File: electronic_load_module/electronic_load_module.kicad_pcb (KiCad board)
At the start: 2 copper layers, 86.9 x 35.3 mm, 66 parts, among them J1 Conn_01x03_Pin, J10 Conn_01x02_Pin, J2 Conn_01x03_Pin, J3 Conn_01x04_Pin, J4 Screw_Terminal_01x02, J5 Screw_Terminal_01x02, J6 Conn_01x05_Pin, J7 Conn_01x04_Pin, J8 Conn_01x04_Pin, J9 Conn_01x04_Pin, Q1 TIP142, Q2 TIP142, Q3 BC549, Q4 BC549, U1 NCS21804, U2 MCP9700Ax-ETT, U3 SN74LV4052, U4 INA180A1, U5 SN74LV4052, U6 NCS21804, U7 INA180A1

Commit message: IDeo ok
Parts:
- removed J1: Conn_01x03_Pin, Connector_PinHeader_2.54mm:PinHeader_1x03_P2.54mm_Vertical
- removed J3: Conn_01x04_Pin, Connector_PinHeader_2.54mm:PinHeader_1x04_P2.54mm_Vertical
- removed J4: Screw_Terminal_01x02, TerminalBlock:TerminalBlock_Altech_AK300-2_P5.00mm
- removed Q1, Q2: TIP142, Package_TO_SOT_THT:TO-247-3_Vertical
- removed Q3: BC549, Package_TO_SOT_THT:TO-92_Inline
- removed R10, R17, R20, R23, R24, R25, R28, R29, R34, R35, R36: 0, Resistor_SMD:R_0603_1608Metric_Pad0.98x0.95mm_HandSolder
- removed R13, R14, R18, R19: 10k, Resistor_SMD:R_0603_1608Metric_Pad0.98x0.95mm_HandSolder
- removed R15, R6: 0.05, Resistor_SMD:R_2512_6332Metric_Pad1.40x3.35mm_HandSolder
- removed R16: 220, Resistor_SMD:R_0603_1608Metric_Pad0.98x0.95mm_HandSolder
- removed R21, R22: 1k, Resistor_SMD:R_0603_1608Metric_Pad0.98x0.95mm_HandSolder
- removed U3: SN74LV4052, Package_SO:SOIC-16_3.9x9.9mm_P1.27mm
- removed U4: INA180A1, Package_TO_SOT_SMD:SOT-23-5
- added C10: 100n, Capacitor_SMD:C_0603_1608Metric_Pad1.08x0.95mm_HandSolder, F.Cu at (58.7, 67.5)
- added J11: Conn_01x03_Pin, Connector_PinHeader_2.54mm:PinHeader_1x03_P2.54mm_Vertical, F.Cu at (50.8, 51.3)
- added Q5: TIP142, Package_TO_SOT_THT:TO-247-3_Vertical, F.Cu at (65.2, 34.8)
- added R43: 1k, Resistor_SMD:R_0603_1608Metric_Pad0.98x0.95mm_HandSolder, F.Cu at (79.0, 46.0)
- added U8: INA180A1, Package_TO_SOT_SMD:SOT-23-5, F.Cu at (60.0, 39.2)
- C1: value 220p -> 100p; moved to F.Cu
- C2, C7: value 10n -> 100n; moved to F.Cu
- C3, C6, J2, R30, R31, R9, U1, U5, U7: moved to F.Cu
- C4: value 100n -> 100p; moved to F.Cu
- C5: value 220p -> 100n; moved to F.Cu
- C8, C9: value 100n -> 220p; moved to F.Cu
- J10: value Conn_01x02_Pin -> Conn_01x05_Pin; footprint Connector_PinHeader_2.54mm:PinHeader_1x02_P2.54mm_Vertical -> Connector_JST:JST_EH_B5B-EH-A_1x05_P2.50mm_Vertical; moved to F.Cu
- J5: value Screw_Terminal_01x02 -> Conn_01x03_Pin; footprint TerminalBlock:TerminalBlock_Altech_AK300-2_P5.00mm -> Connector_JST:JST_EH_B3B-EH-A_1x03_P2.50mm_Vertical; moved to F.Cu
- J6: footprint Connector_PinHeader_2.54mm:PinHeader_1x05_P2.54mm_Vertical -> Connector_JST:JST_EH_B5B-EH-A_1x05_P2.50mm_Vertical; moved to F.Cu
- J7: value Conn_01x04_Pin -> Conn_01x03_Pin; footprint Connector_PinHeader_2.54mm:PinHeader_1x04_P2.54mm_Vertical -> Connector_JST:JST_EH_B3B-EH-A_1x03_P2.50mm_Vertical; moved to F.Cu
- J8, J9: value Conn_01x04_Pin -> Conn_01x02_Socket; footprint Connector_PinHeader_2.54mm:PinHeader_1x04_P2.54mm_Vertical -> Connector_JST:JST_EH_B2B-EH-A_1x02_P2.50mm_Vertical; moved to F.Cu
- Q4: value BC549 -> TIP142; footprint Package_TO_SOT_THT:TO-92_Inline -> Package_TO_SOT_THT:TO-247-3_Vertical; moved to F.Cu
- R1, R26, R27: value 0 -> 10k; moved to F.Cu
- R11: value 0 -> 220; moved to F.Cu
- R12: value 1k -> 0; moved to F.Cu
- R2: value 10k -> 90k; moved to F.Cu
- R3: value 220 -> 3.3k; moved to F.Cu
- R32, R33: value 0 -> 0.05; footprint Resistor_SMD:R_0603_1608Metric_Pad0.98x0.95mm_HandSolder -> Resistor_SMD:R_2512_6332Metric_Pad1.40x3.35mm_HandSolder; moved to F.Cu
- R4: value 280k -> 6.6k; moved to F.Cu
- R5: value 0 -> 100; moved to F.Cu
- R7: value 20k -> 10k; moved to F.Cu
- R8: value 10k -> 220; moved to F.Cu
- U2: value MCP9700Ax-ETT -> TLV07; footprint Package_TO_SOT_THT:TO-92_Inline -> Package_SO:SOIC-8_3.9x4.9mm_P1.27mm
- U6: value NCS21804 -> SN74LV4052; footprint Package_SO:TSSOP-14_4.4x5mm_P0.65mm -> Package_SO:SOIC-16_3.9x9.9mm_P1.27mm; moved to F.Cu
- moved U6 142.1 mm to (50.6, 45.6), turned to -90 degrees
- moved J6 136.9 mm to (35.5, 51.9), turned to 90 degrees
- moved C5 136.2 mm to (54.4, 50.2), turned to 180 degrees
- moved R27 135.0 mm to (52.4, 39.2)
- moved R30 131.9 mm to (45.1, 39.2), turned to 180 degrees
- moved C8 131.3 mm to (65.8, 45.5), turned to 0 degrees
- moved C7 130.3 mm to (60.0, 43.5), turned to 0 degrees
- moved C9 128.7 mm to (48.8, 39.2), turned to 180 degrees
- moved R8 126.1 mm to (65.8, 48.6)
- moved J5 124.4 mm to (45.2, 71.0), turned to 90 degrees
- moved U2 119.9 mm to (63.4, 64.8), turned to 0 degrees
- moved R26 109.9 mm to (72.2, 40.0), turned to 90 degrees
- moved U5 109.5 mm to (72.8, 45.9), turned to -90 degrees
- moved J7 106.2 mm to (67.0, 57.8)
- moved R11 106.2 mm to (41.4, 42.6), turned to 0 degrees
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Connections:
- C1 pad 1: Net-(U1C--) -> Net-(U1C-+)
- C1 pad 2: Net-(C1-Pad2) -> 0
- C2 pad 1: Net-(U1B-+) -> 5V
- C4 pad 1: 5V -> Net-(U1B-+)
- C5 pad 1: Net-(U5-Y) -> 5V
- C5 pad 2: Net-(C5-Pad2) -> 0
- C7 pad 1: Net-(U6B-+) -> 5V
- C8 pad 1: 5V -> Net-(U1D--)
- C8 pad 2: 0 -> Net-(C8-Pad2)
- C9 pad 1: 5V -> Net-(U1A--)
- C9 pad 2: 0 -> Net-(C9-Pad2)
- J10 pad 2: 0 -> COMMON_MUX_A
- J2 pad 1: DAC_from_board -> DAC_2
- J2 pad 2: ADC_SHUNT -> Net-(J2-Pin_2)
- J2 pad 3: ENABLE -> MIXER
- J5 pad 1: 0 -> input_10
- J5 pad 2: input -> input_1000
- J6 pad 1: COMMON_MUX_A -> 5V
- J6 pad 2: COMMON_MUX_B -> COMMON_MUX_A
- J6 pad 3: TEMP -> COMMON_MUX_B
- J6 pad 5: DIVIDER -> 0
- J7 pad 1: DAC_2 -> input_sense
- J7 pad 2: Net-(J7-Pin_2) -> unconnected-(J7-Pin_2-Pad2)
- J8 pad 1: SHUNT -> DAC_from_board
- J8 pad 2: Net-(J8-Pin_2) -> SHUNT
- J9 pad 1: DAC -> DAC_from_board_2
- J9 pad 2: Net-(J9-Pin_2) -> SHUNT_2
- Q4 pad 1: Net-(Q1-B) -> Net-(Q4-B)
- Q4 pad 2: Net-(Q4-B) -> input
- Q4 pad 3: 0 -> Net-(Q4-E)
- R1 pad 1: Net-(C1-Pad2) -> 0
- R1 pad 2: Net-(Q1-B) -> DAC
- R11 pad 1: Net-(U1B--) -> DAC_from_board
- R11 pad 2: DAC -> Net-(U1B-+)
- R12 pad 1: 0 -> Net-(U1B--)
- R12 pad 2: DIVIDER -> DAC
- R2 pad 1: 0 -> input_sense
- R2 pad 2: ADC_SHUNT -> input_10
- R26 pad 1: DAC_2 -> SHUNT_2
- R26 pad 2: Net-(J3-Pin_3) -> Net-(U1D--)
- R27 pad 1: SHUNT_2 -> SHUNT
- R27 pad 2: Net-(J3-Pin_4) -> Net-(U1A--)
- R3 pad 1: DAC_from_board -> input_10
- R3 pad 2: Net-(U1B-+) -> DIVIDER_R
- R30 pad 1: DAC_2 -> Net-(C9-Pad2)
- R30 pad 2: Net-(J7-Pin_4) -> Net-(Q4-B)
- R31 pad 1: DIVIDER -> Net-(C8-Pad2)
- R31 pad 2: Net-(J9-Pin_2) -> Net-(Q5-B)
- R32 pad 1: DIVIDER -> Net-(Q4-E)
- R32 pad 2: Net-(J9-Pin_3) -> 0
- R33 pad 1: DAC -> Net-(Q5-E)
- R33 pad 2: Net-(J9-Pin_4) -> 0
- R4 pad 1: input_sense -> DIVIDER_R
- R4 pad 2: input_divider -> input_1000
- R5 pad 1: ADC_SHUNT -> input_1000
- R5 pad 2: Net-(U1D--) -> Net-(J7-Pin_3)
- R7 pad 1: input_divider -> 0
- R7 pad 2: 0 -> DAC_2
- R8 pad 1: SHUNT_2 -> DAC_from_board_2
- R8 pad 2: Net-(U5-Y) -> Net-(U1C-+)
- R9 pad 1: Net-(U1A--) -> Net-(U1C--)
- R9 pad 2: DIVIDER -> DAC_2
- U1 pad 1: DIVIDER -> Net-(C9-Pad2)
- U1 pad 12: SHUNT -> Net-(U1D-+)
- U1 pad 14: ADC_SHUNT -> Net-(C8-Pad2)
- U1 pad 3: input_divider -> Net-(U1A-+)
- U1 pad 8: Net-(C1-Pad2) -> DAC_2
- U2 pad 1: 5V -> (no net)
- U2 pad 2: Net-(U2-V_{OUT}) -> DIVIDER
- U2 pad 3: 0 -> DIVIDER_R
- U5 pad 11: Net-(J7-Pin_4) -> Net-(J2-Pin_2)
- U5 pad 13: Net-(U5-X) -> Net-(U1D-+)
- U5 pad 14: Net-(J7-Pin_2) -> Net-(J2-Pin_2)
- U5 pad 15: Net-(J7-Pin_3) -> DIVIDER
- U5 pad 2: Net-(J3-Pin_3) -> DAC_2
- U5 pad 3: Net-(U5-Y) -> Net-(U1D--)
- U5 pad 4: Net-(J3-Pin_4) -> SHUNT_2
- U5 pad 5: Net-(J3-Pin_2) -> SHUNT_2
- U6 pad 1: TEMP -> SHUNT
- U6 pad 10: Net-(U5-X) -> COMMON_MUX_A
- U6 pad 11: 0 -> Net-(J11-Pin_2)
- U6 pad 12: SHUNT_2 -> DAC
- U6 pad 13: Net-(U6D--) -> Net-(U1A-+)
- U6 pad 14: ADC_SHUNT_2 -> Net-(J11-Pin_2)
- U6 pad 2: Net-(U6A--) -> DAC
- U6 pad 3: Net-(U6A-+) -> Net-(U1A--)
- U6 pad 4: 5V -> SHUNT
- U6 pad 5: Net-(U6B-+) -> SHUNT
- U6 pad 6: Net-(U6B--) -> 0
- U6 pad 7: DAC_2 -> 0
- U6 pad 8: Net-(C5-Pad2) -> 0
- U6 pad 9: Net-(U5-Y) -> COMMON_MUX_B
- U7 pad 1: SHUNT -> SHUNT_2
- U7 pad 3: Net-(Q1-E) -> Net-(Q5-E)
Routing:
- net 5V: track 148.7 -> 0.00 mm, vias 7 -> 0
- net DIVIDER: track 84.0 -> 0.00 mm, vias 4 -> 0
- net COMMON_MUX_A: track 65.8 -> 0.00 mm, vias 3 -> 0
- net Net-(Q2-E): track 57.6 -> 0.00 mm
- net COMMON_MUX_B: track 55.7 -> 0.00 mm, vias 1 -> 0
- net SHUNT: track 43.3 -> 0.00 mm, vias 3 -> 0
- net DAC: track 35.5 -> 0.00 mm, vias 3 -> 0
- net DAC_2: track 34.5 -> 0.00 mm
- net SHUNT_2: track 32.5 -> 0.00 mm, vias 4 -> 0
- net TEMP: track 28.3 -> 0.00 mm, vias 1 -> 0
- net Net-(U2-V_{OUT}): track 25.5 -> 0.00 mm
- net Net-(U1C-+): track 24.0 -> 0.00 mm, vias 2 -> 0
- net Net-(J9-Pin_4): track 21.9 -> 0.00 mm
- net Net-(Q1-E): track 21.1 -> 0.00 mm, vias 1 -> 0
- net Net-(U1C--): track 18.7 -> 0.00 mm, vias 2 -> 0
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- removed copper zone on B.Cu, net 0
- removed copper zone on F.Cu, net 0
- removed copper zone on B.Cu, net Net-(Q1-E)
- removed copper zone on F.Cu, net Net-(Q1-E)
- removed copper zone on B.Cu, net Net-(Q2-E)
- removed copper zone on F.Cu, net Net-(Q2-E)
- removed copper zone on B.Cu, net input
- removed copper zone on F.Cu, net input
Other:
- board outline removed

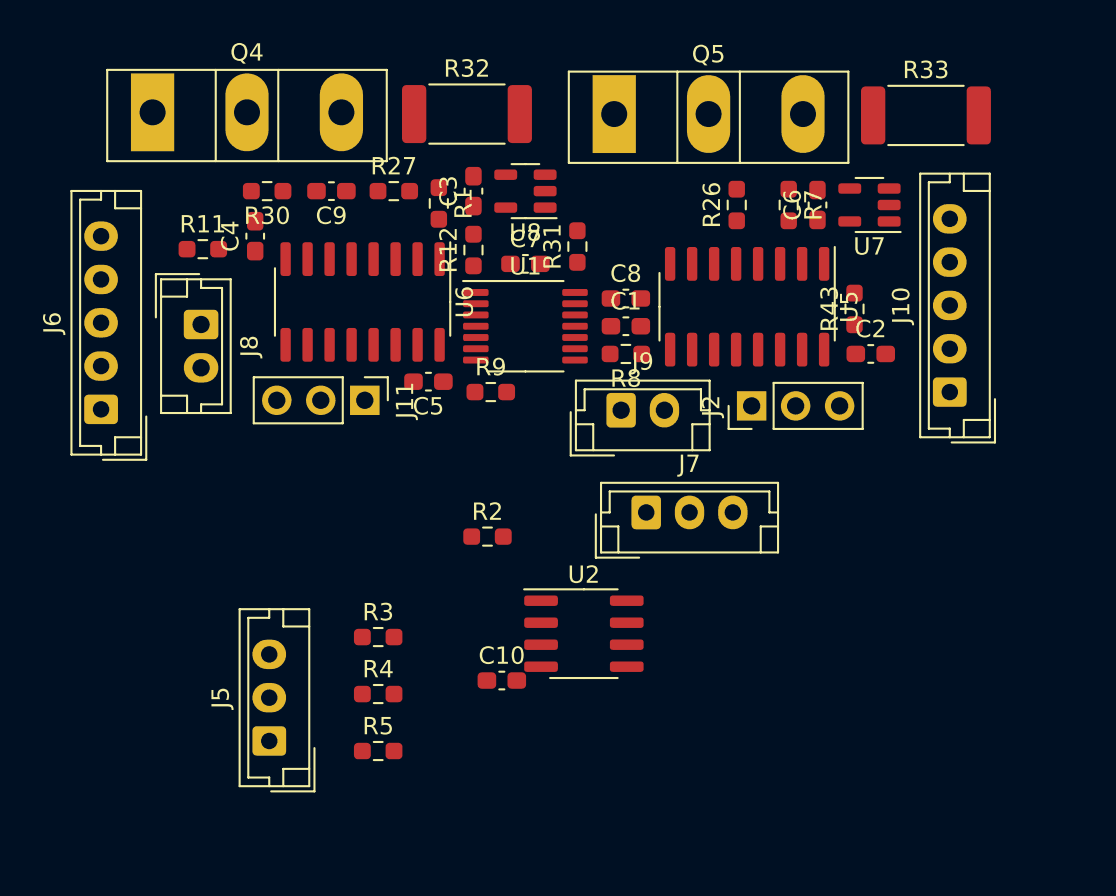
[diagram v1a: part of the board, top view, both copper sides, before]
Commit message: Konačno PCB za BJT modul je počeo.
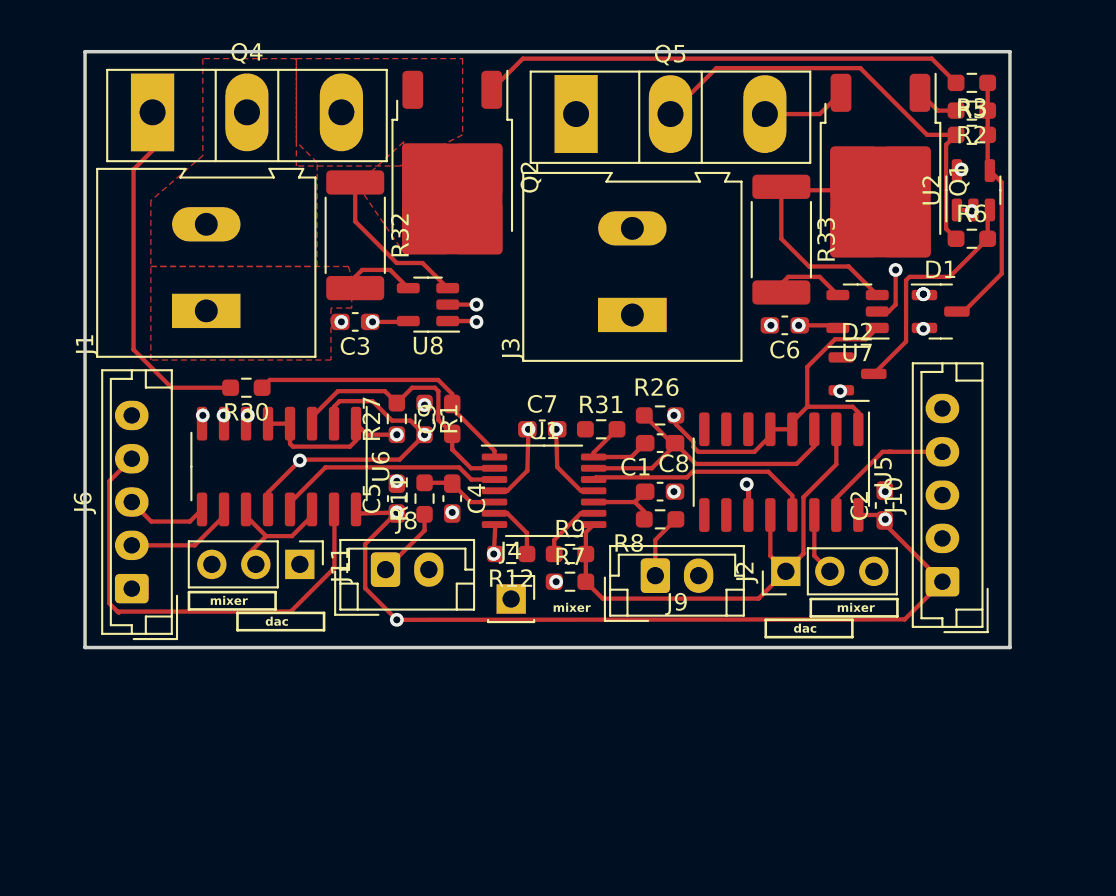
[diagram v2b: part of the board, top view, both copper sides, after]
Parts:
- removed C10: 100n, Capacitor_SMD:C_0603_1608Metric_Pad1.08x0.95mm_HandSolder
- removed J5, J7: Conn_01x03_Pin, Connector_JST:JST_EH_B3B-EH-A_1x03_P2.50mm_Vertical
- removed R4: 6.6k, Resistor_SMD:R_0603_1608Metric_Pad0.98x0.95mm_HandSolder
- removed R43: 1k, Resistor_SMD:R_0603_1608Metric_Pad0.98x0.95mm_HandSolder
- added D1: BAT54S, Package_TO_SOT_SMD:SOT-23, F.Cu at (84.0, 46.2)
- added D2: BAT54S, Package_TO_SOT_SMD:SOT-23, F.Cu at (79.2, 49.8)
- added J1: Screw_Terminal_01x02, TerminalBlock:TerminalBlock_Altech_AK300-2_P5.00mm, F.Cu at (41.6, 46.2)
- added J3: Screw_Terminal_01x02, TerminalBlock:TerminalBlock_Altech_AK300-2_P5.00mm, F.Cu at (66.2, 46.4)
- added J4: Conn_01x01_Socket, Connector_PinSocket_2.54mm:PinSocket_1x01_P2.54mm_Vertical, F.Cu at (59.2, 62.8)
- added Q1: DMT10H025SK3-13, Package_TO_SOT_SMD:TO-252-2, F.Cu at (80.5, 38.6)
- added Q2: DMT10H025SK3-13, Package_TO_SOT_SMD:TO-252-2, F.Cu at (55.8, 38.4)
- added R6: 10k, Resistor_SMD:R_0603_1608Metric_Pad0.98x0.95mm_HandSolder, F.Cu at (85.8, 42.0)
- C1, C4: value 100p -> 1n
- R2: value 90k -> 100
- R3: value 3.3k -> 100
- R30, R31: value 0 -> 3.3k
- R5: value 100 -> 10k
- U2: value TLV07 -> MCP6541; footprint Package_SO:SOIC-8_3.9x4.9mm_P1.27mm -> Package_TO_SOT_SMD:SOT-23-5
- moved R5 49.4 mm to (85.8, 36.0)
- moved R3 46.9 mm to (85.8, 33.0), turned to 180 degrees
- moved R2 37.2 mm to (85.8, 34.6), turned to 180 degrees
- moved U2 34.1 mm to (85.9, 39.2), turned to 90 degrees
- moved R7 25.1 mm to (62.6, 61.8), turned to 0 degrees
- moved R11 19.3 mm to (54.2, 57.0), turned to 90 degrees
- moved C4 18.9 mm to (55.8, 57.0), turned to -90 degrees
- moved J8 17.7 mm to (52.0, 61.1), turned to 0 degrees
- moved R12 17.7 mm to (59.2, 60.2), turned to 180 degrees
- moved C9 14.9 mm to (55.8, 52.4), turned to 90 degrees
- moved R27 13.2 mm to (52.6, 52.4), turned to 90 degrees
- moved R26 12.9 mm to (67.8, 52.2), turned to 180 degrees
- moved R1 12.5 mm to (54.2, 52.4)
- moved R30 11.4 mm to (43.9, 50.6)
- moved R33 11.0 mm to (74.8, 42.0), turned to -90 degrees
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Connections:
- Q4 pad 3: Net-(Q4-E) -> Net-(Q2-S)
- Q5 pad 3: Net-(Q5-E) -> Net-(Q1-S)
- R2 pad 1: input_sense -> P_GATE
- R2 pad 2: input_10 -> Net-(Q1-G)
- R3 pad 1: input_10 -> P_GATE
- R3 pad 2: DIVIDER_R -> Net-(Q2-G)
- R32 pad 1: Net-(Q4-E) -> Net-(Q2-D)
- R33 pad 1: Net-(Q5-E) -> Net-(Q1-D)
- R5 pad 1: input_1000 -> input
- R5 pad 2: Net-(J7-Pin_3) -> P_GATE
- U2 pad 1: (no net) -> 0
- U2 pad 2: DIVIDER -> 0
- U2 pad 3: DIVIDER_R -> Net-(D2-COM)
- U2 pad 4: 0 -> P_GATE
- U2 pad 5: (no net) -> 5V
- U7 pad 3: Net-(Q5-E) -> Net-(Q1-D)
- U8 pad 3: Net-(Q4-E) -> Net-(Q2-D)
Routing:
- net 5V: track 0.00 -> 167.1 mm, vias 0 -> 8
- net DIVIDER: track 0.00 -> 82.9 mm
- net COMMON_MUX_A: track 0.00 -> 53.9 mm
- net COMMON_MUX_B: track 0.00 -> 52.0 mm
- net MIXER: track 0.00 -> 39.7 mm
- net DAC: track 0.00 -> 36.1 mm, vias 0 -> 3
- net SHUNT_2: track 0.00 -> 31.8 mm, vias 0 -> 1
- net DAC_2: track 0.00 -> 29.4 mm
- net SHUNT: track 0.00 -> 28.9 mm, vias 0 -> 2
- net Net-(Q2-G): track 0.00 -> 28.1 mm
- net input: track 0.00 -> 25.4 mm
- net Net-(Q4-B): track 0.00 -> 20.7 mm
- net 0: track 0.00 -> 19.5 mm, vias 0 -> 18
- net Net-(U1D--): track 0.00 -> 17.7 mm
- net Net-(C9-Pad2): track 0.00 -> 16.1 mm
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- added copper zone on B.Cu, net 0
- added copper zone on F.Cu, net 0
- added copper zone on F.Cu, net Net-(Q2-D)
- added copper zone on F.Cu, net Net-(Q2-S)
- added copper zone on F.Cu, net input
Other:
- board outline added: 53.4 x 34.4 mm
- copper layers 2 -> 4
- board text added: "dac"
- board text added: "mixer"
